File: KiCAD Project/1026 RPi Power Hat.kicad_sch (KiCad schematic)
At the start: 0 parts

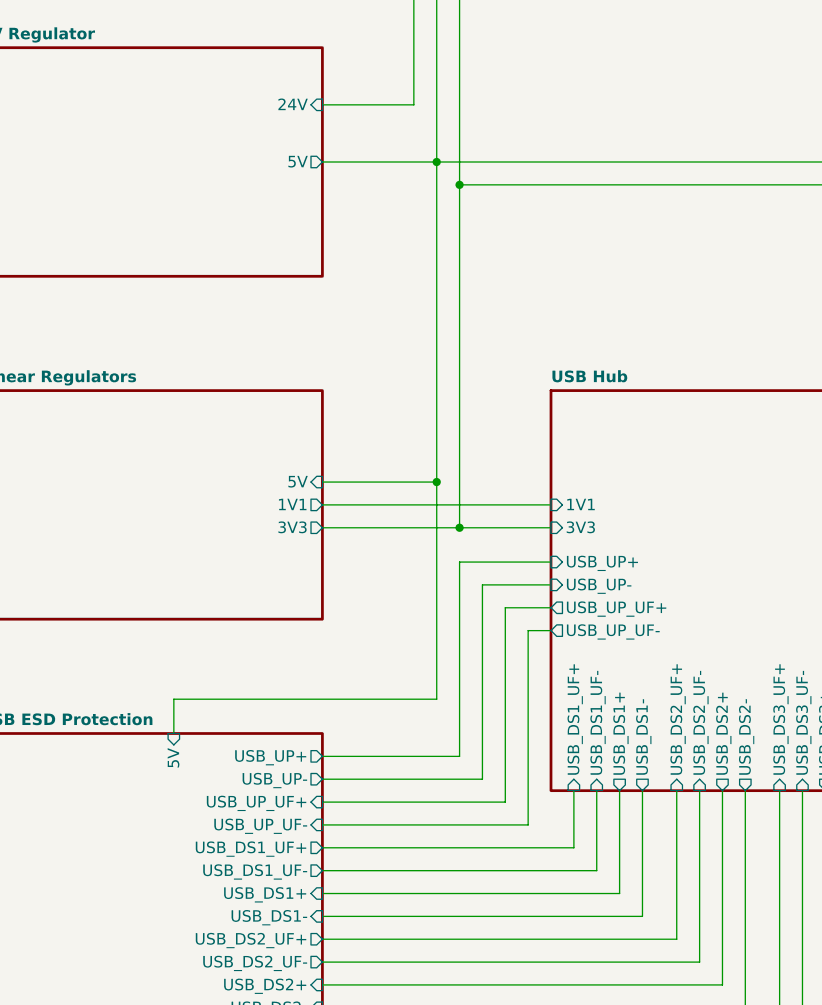
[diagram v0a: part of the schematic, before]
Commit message: v1.0.0 RC3
Minor change to upstream USB port to connect Vbus to ESD protection vice on-board 5V.
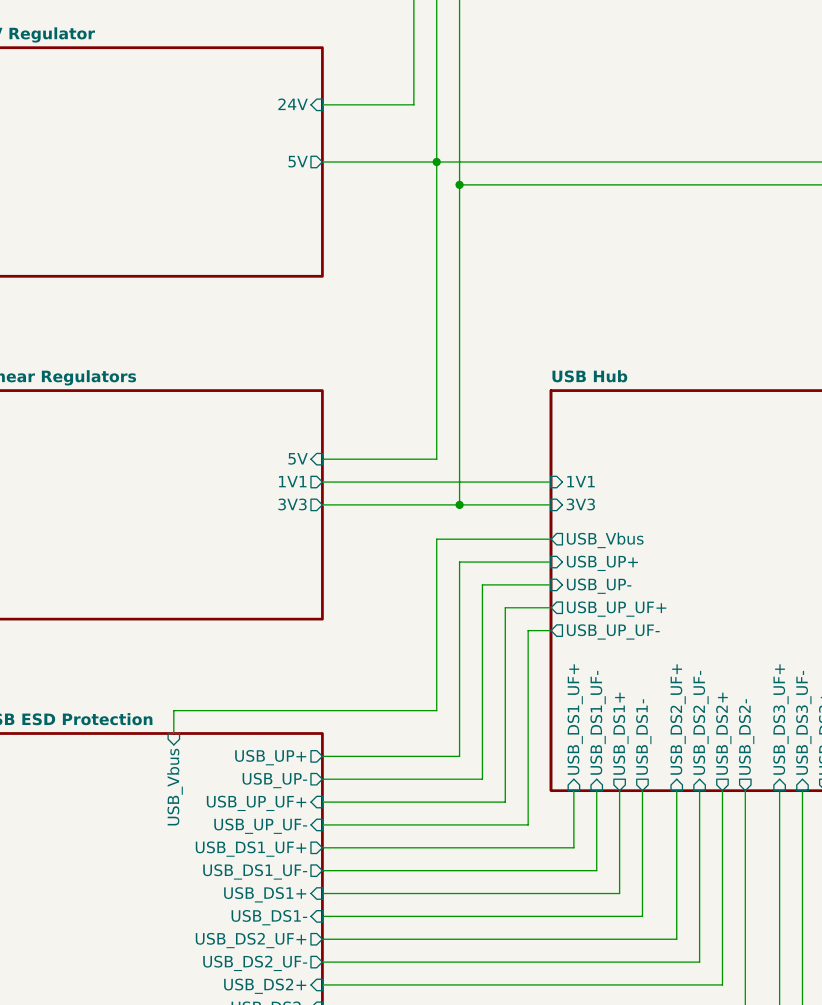
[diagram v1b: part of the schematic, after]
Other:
- sheet USB ESD Protection ports: added USB_Vbus; removed 5V
- sheet USB Hub ports: added USB_Vbus; removed none
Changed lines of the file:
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@@
 		(title "1026 RPi Power Hat")
 		(date "2025-04-11")
-		(rev "1")
+		(rev "1.0.0 RC3")
 		(company "Dan Wilson")
 		(comment 1 "Copyright © 2025 Dan Wilson")
@@
 	)
 	(junction
-		(at 88.9 111.76)
+		(at 91.44 114.3)
 		(diameter 0)
 		(color 0 0 0 0)
@@
 		(color 0 0 0 0)
 	)
-	(junction
-		(at 91.44 116.84)
-		(diameter 0)
-		(color 0 0 0 0)
-	)
 	(wire
 		(pts
@@
 	(wire
 		(pts
-			(xy 59.69 135.89) (xy 88.9 135.89)
-		)
-		(stroke
-			(width 0)
-			(type default)
-		)
-	)
-	(wire
-		(pts
-			(xy 76.2 116.84) (xy 91.44 116.84)
+			(xy 76.2 114.3) (xy 91.44 114.3)
 		)
 		(stroke
@@
 	(wire
 		(pts
-			(xy 88.9 111.76) (xy 88.9 135.89)
-		)
-		(stroke
-			(width 0)
-			(type default)
-		)
-	)
-	(wire
-		(pts
 			(xy 76.2 182.88) (xy 138.43 182.88)
 		)
@@
 	(wire
 		(pts
-			(xy 76.2 114.3) (xy 101.6 114.3)
+			(xy 76.2 111.76) (xy 101.6 111.76)
 		)
 		(stroke
@@
 	(wire
 		(pts
-			(xy 91.44 78.74) (xy 91.44 116.84)
+			(xy 91.44 78.74) (xy 91.44 114.3)
 		)
 		(stroke
@@
 	(wire
 		(pts
-			(xy 76.2 111.76) (xy 88.9 111.76)
+			(xy 76.2 109.22) (xy 88.9 109.22)
+		)
+		(stroke
+			(width 0)
+			(type default)
+		)
+	)
+	(wire
+		(pts
+			(xy 88.9 137.16) (xy 59.69 137.16)
 		)
 		(stroke
@@
 	(wire
 		(pts
-			(xy 59.69 139.7) (xy 59.69 135.89)
+			(xy 88.9 118.11) (xy 88.9 137.16)
 		)
 		(stroke
@@
 	(wire
 		(pts
-			(xy 91.44 116.84) (xy 101.6 116.84)
+			(xy 91.44 114.3) (xy 101.6 114.3)
+		)
+		(stroke
+			(width 0)
+			(type default)
+		)
+	)
+	(wire
+		(pts
+			(xy 59.69 137.16) (xy 59.69 139.7)
 		)
 		(stroke
@@
 	(wire
 		(pts
-			(xy 88.9 76.2) (xy 88.9 111.76)
+			(xy 88.9 76.2) (xy 88.9 109.22)
 		)
 		(stroke
@@
 		(pts
 			(xy 165.1 129.54) (xy 203.2 129.54)
+		)
+		(stroke
+			(width 0)
+			(type default)
+		)
+	)
+	(wire
+		(pts
+			(xy 101.6 118.11) (xy 88.9 118.11)
 		)
 		(stroke
@@
 		)
 		(pin "1V1" input
+			(at 101.6 111.76 180)
+			(effects
+				(font
+					(size 1.27 1.27)
+				)
+				(justify left)
+			)
+		)
+		(pin "3V3" input
 			(at 101.6 114.3 180)
-			(effects
-				(font
-					(size 1.27 1.27)
-				)
-				(justify left)
-			)
-		)
-		(pin "3V3" input
-			(at 101.6 116.84 180)
 			(effects
 				(font
@@
 		(pin "USB_UP_UF+" output
 			(at 101.6 125.73 180)
+			(effects
+				(font
+					(size 1.27 1.27)
+				)
+				(justify left)
+			)
+		)
+		(pin "USB_Vbus" output
+			(at 101.6 118.11 180)
 			(effects
 				(font
@@
 		)
 		(pin "5V" input
+			(at 76.2 109.22 0)
+			(effects
+				(font
+					(size 1.27 1.27)
+				)
+				(justify right)
+			)
+		)
+		(pin "1V1" output
 			(at 76.2 111.76 0)
 			(effects
@@
 			)
 		)
-		(pin "1V1" output
+		(pin "3V3" output
 			(at 76.2 114.3 0)
-			(effects
-				(font
-					(size 1.27 1.27)
-				)
-				(justify right)
-			)
-		)
-		(pin "3V3" output
-			(at 76.2 116.84 0)
 			(effects
 				(font
@@
 			)
 		)
-		(pin "5V" input
-			(at 59.69 139.7 90)
-			(effects
-				(font
-					(size 1.27 1.27)
-				)
-				(justify right)
-			)
-		)
 		(pin "USB_DS1+" input
 			(at 76.2 157.48 0)
@@
 			)
 		)
+		(pin "USB_Vbus" input
+			(at 59.69 139.7 90)
+			(effects
+				(font
+					(size 1.27 1.27)
+				)
+				(justify right)
+			)
+		)
